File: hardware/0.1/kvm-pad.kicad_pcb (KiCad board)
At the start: 2 copper layers, 76.2 x 64.1 mm, 93 parts, among them J1 USB_C_Receptacle_USB2.0, J2 USB_C_Receptacle_USB2.0, J3 AVR-ISP-6, J4 USB_A, J5 USB_A, J6 USB_A, K1 KEYSW, K2 KEYSW, K3 KEYSW, K4 KEYSW, K5 KEYSW, K6 KEYSW, K7 KEYSW, K8 KEYSW, U1 USBLC6-2SC6, U2 ATMEGA32U4, U3 USBLC6-2SC6, U4 TPS211x, U5 TS3USB30, U6 CY7C65632-28LTXCT, Y1 16MHz, Y2 12MHz

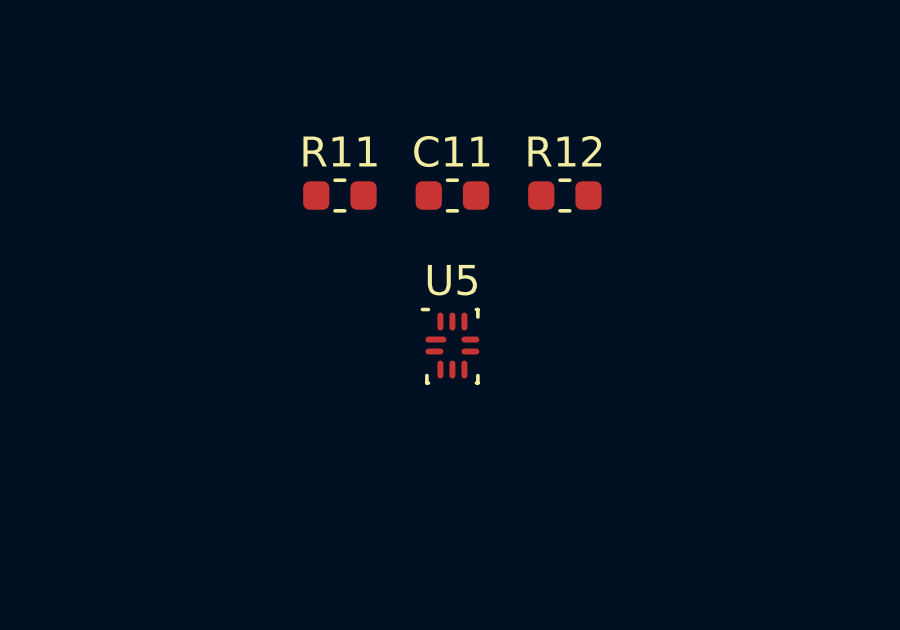
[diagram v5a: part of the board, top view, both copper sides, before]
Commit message: Switch to VSON TS3USB221E for easier routing
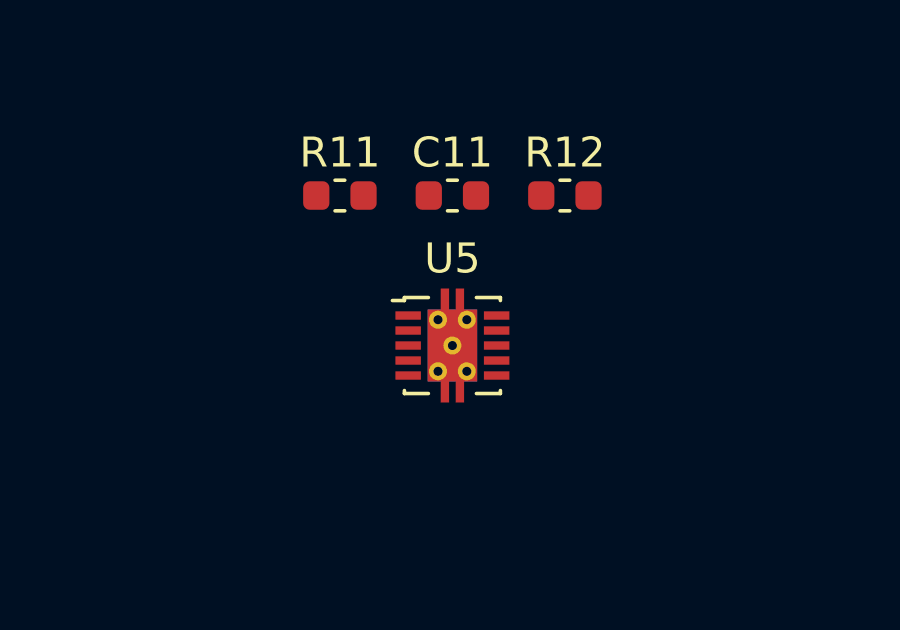
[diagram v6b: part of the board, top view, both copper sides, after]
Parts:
- U5: value TS3USB30 -> TS3USB221E; footprint josh-dfn-qfn:UQFN-10_1.4x1.8_Pitch0.4mm -> Package_SON:VSON-10-1EP_3x3mm_P0.5mm_EP1.65x2.4mm_ThermalVias
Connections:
- U5 pad 10: Net-(R10-Pad1) -> +3.3VA
- U5 pad 2: /USB_2_D+ -> /USB_1_D-
- U5 pad 3: /usb/UP_USB_P -> /USB_2_D+
- U5 pad 4: GND -> /USB_2_D-
- U5 pad 5: /usb/UP_USB_N -> GND
- U5 pad 6: /USB_2_D- -> Net-(R12-Pad1)
- U5 pad 7: /USB_1_D- -> /usb/UP_USB_N
- U5 pad 8: Net-(R12-Pad1) -> /usb/UP_USB_P
- U5 pad 9: +3.3VA -> Net-(R10-Pad1)

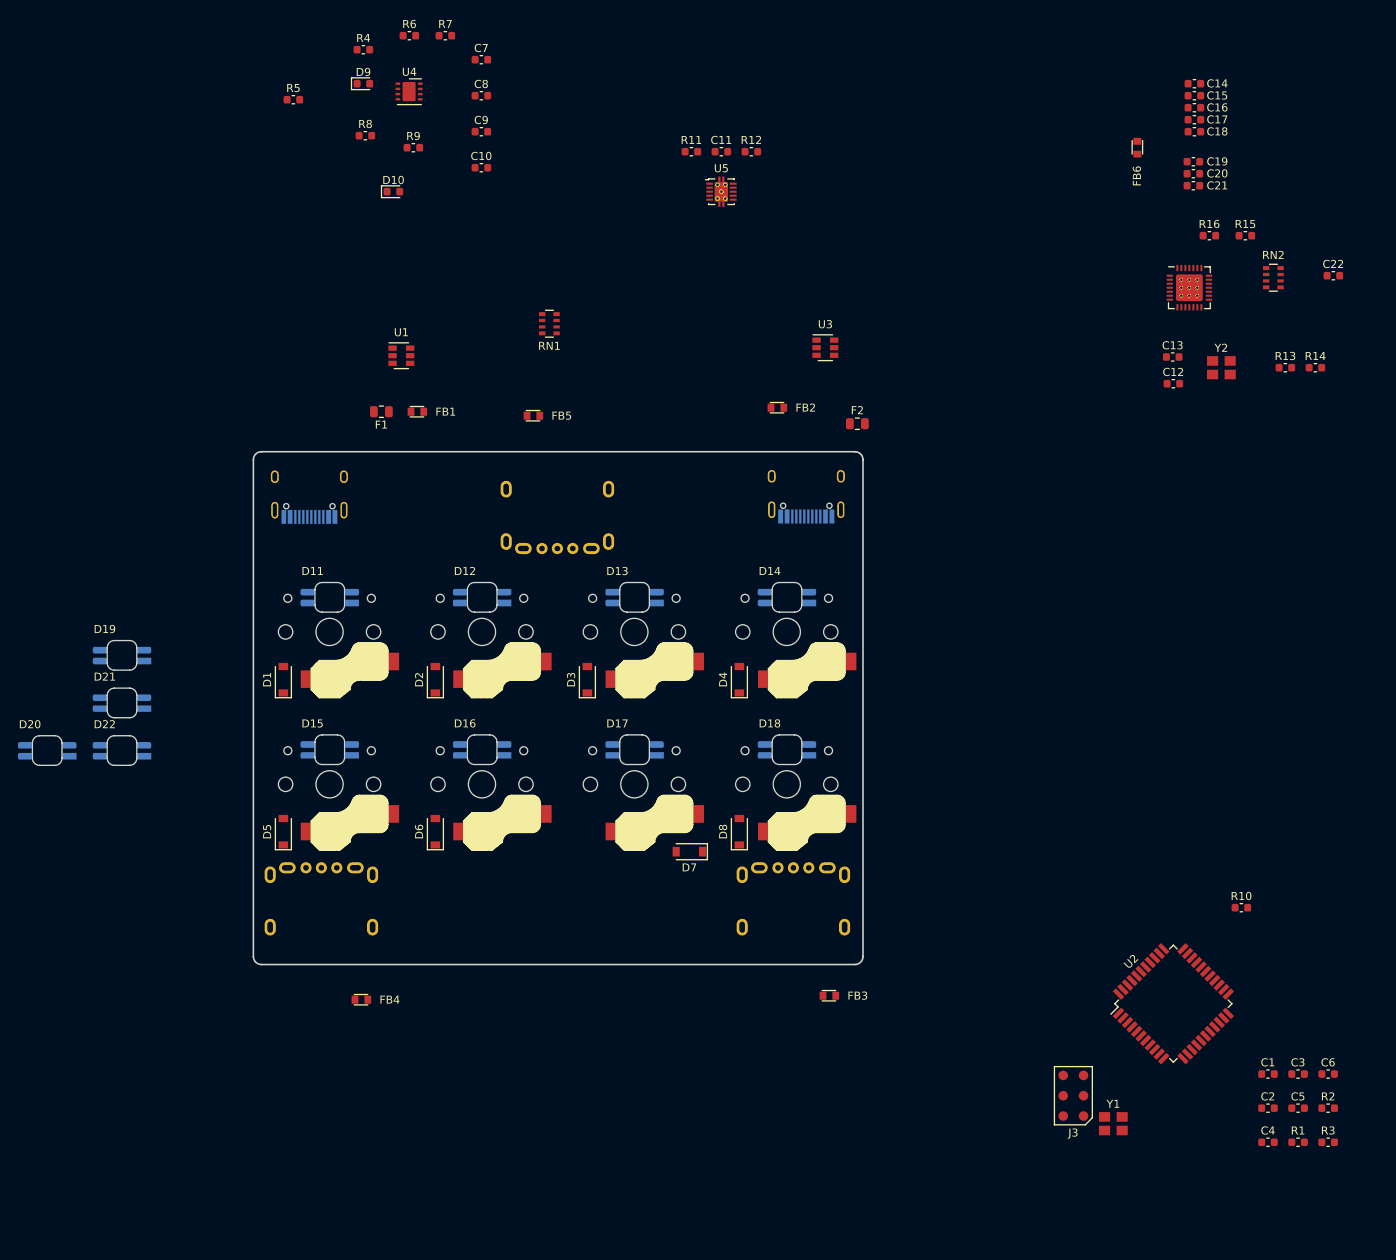
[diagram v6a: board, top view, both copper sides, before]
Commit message: [pcb] Switch routing
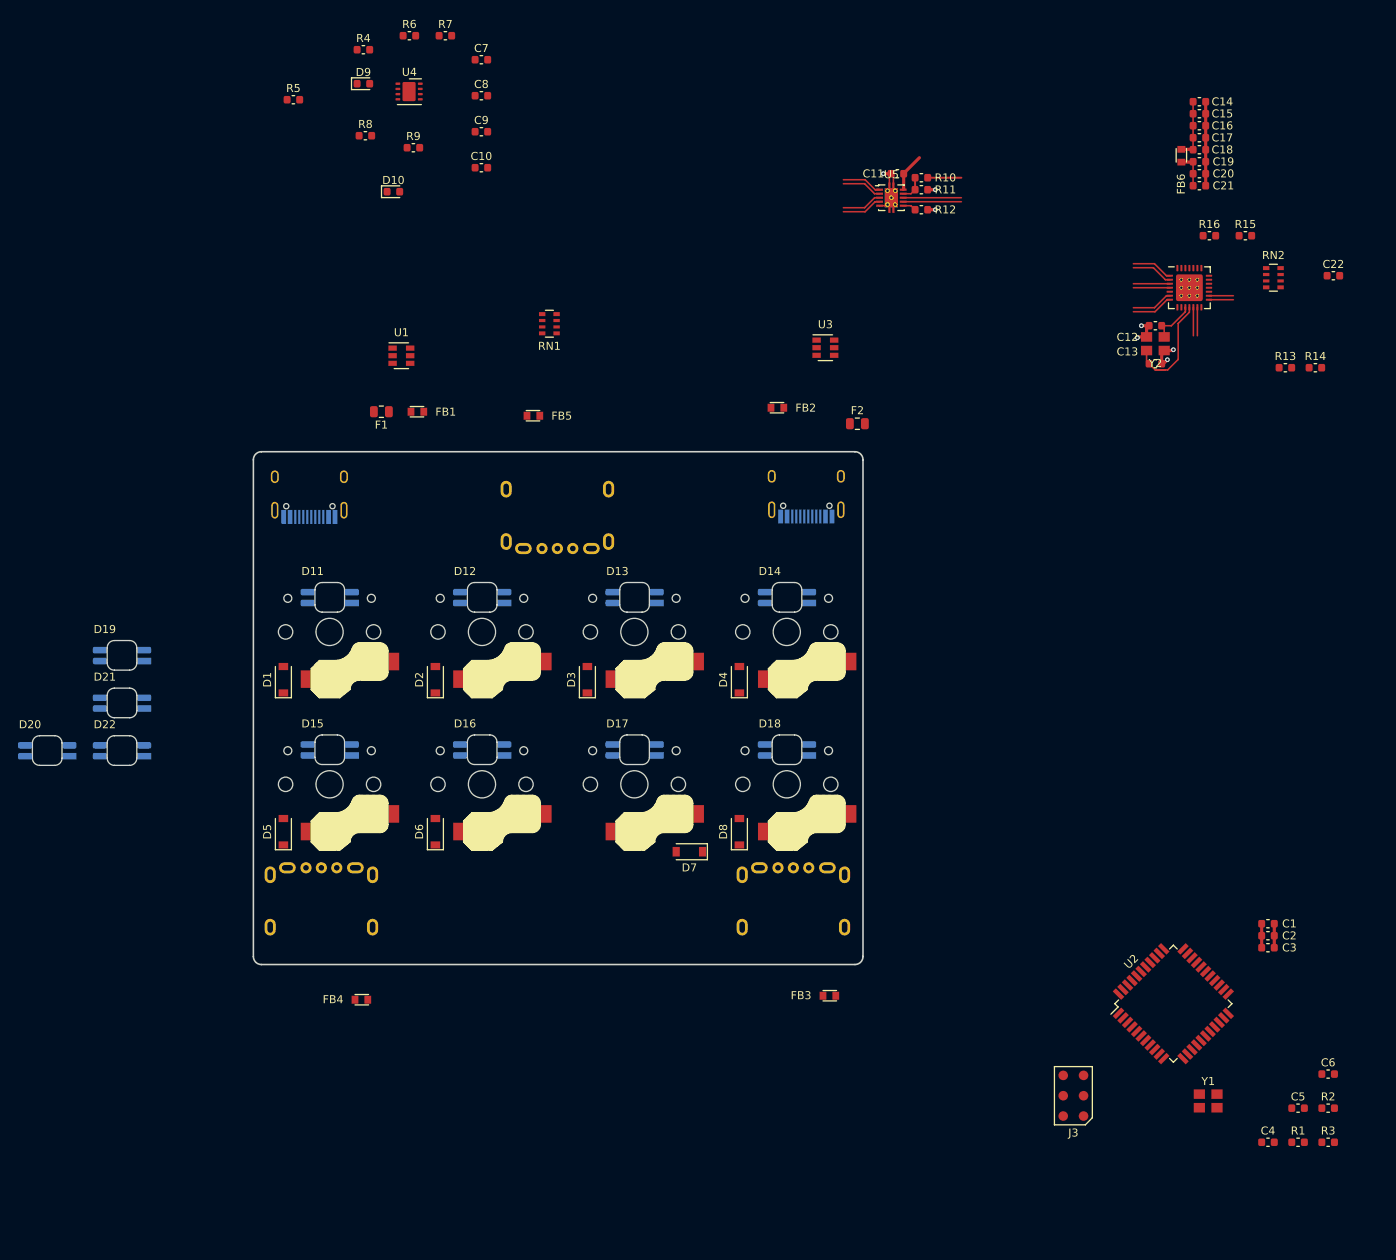
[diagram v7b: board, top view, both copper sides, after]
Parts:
- moved R10 99.6 mm to (83.5, -34.2)
- moved R11 29.1 mm to (83.5, -32.8), turned to 180 degrees
- moved R12 22.5 mm to (83.5, -30.2)
- moved C11 22.2 mm to (80.5, -34.8)
- moved C2 21.6 mm to (126.8, 60.5)
- moved U5 21.3 mm to (79.8, -31.8)
- moved C1 18.8 mm to (126.8, 59.0)
- moved C3 16.2 mm to (126.8, 62.0)
- moved Y1 12.2 mm to (119.3, 81.2)
- moved Y2 8.78 mm to (112.8, -13.5), turned to 180 degrees
- moved C12 7.59 mm to (112.8, -15.8), turned to 180 degrees
- moved FB6 5.59 mm to (116.0, -37.0)
- moved C14 2.33 mm to (118.2, -43.8)
- moved C15 2.33 mm to (118.2, -42.2)
- moved C16 2.33 mm to (118.2, -40.8)
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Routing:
- net GND: track 0.00 -> 29.1 mm, vias 0 -> 7
- net /usb/XOUT: track 0.00 -> 14.6 mm
- net /usb/UP_USB_P: track 0.00 -> 12.4 mm
- net /usb/UP_USB_N: track 0.00 -> 12.4 mm
- net +3.3VA: track 0.00 -> 12.3 mm
- net /usb/XIN: track 0.00 -> 5.99 mm
- net /USB_1_D+: track 0.00 -> 5.44 mm
- net /usb/D2_D-: track 0.00 -> 5.17 mm
- net /usb/D2_D+: track 0.00 -> 5.17 mm
- net /USB_2_D-: track 0.00 -> 5.04 mm
- net /USB_2_D+: track 0.00 -> 5.04 mm
- net /USB_1_D-: track 0.00 -> 5.04 mm
- net /usb/D1_D-: track 0.00 -> 4.55 mm
- net /usb/D1_D+: track 0.00 -> 4.55 mm
- net +3V3: track 0.00 -> 4.48 mm
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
